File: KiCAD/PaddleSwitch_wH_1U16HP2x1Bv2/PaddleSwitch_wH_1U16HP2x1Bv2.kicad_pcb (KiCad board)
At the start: 2 copper layers, 80.9 x 39.7 mm, 13 parts, among them SW1 SW_DPDT-p5xp6i_Panel_Mount_Pa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, SW2 SW_DPDT-p5xp6i_Panel_Mount_Pa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

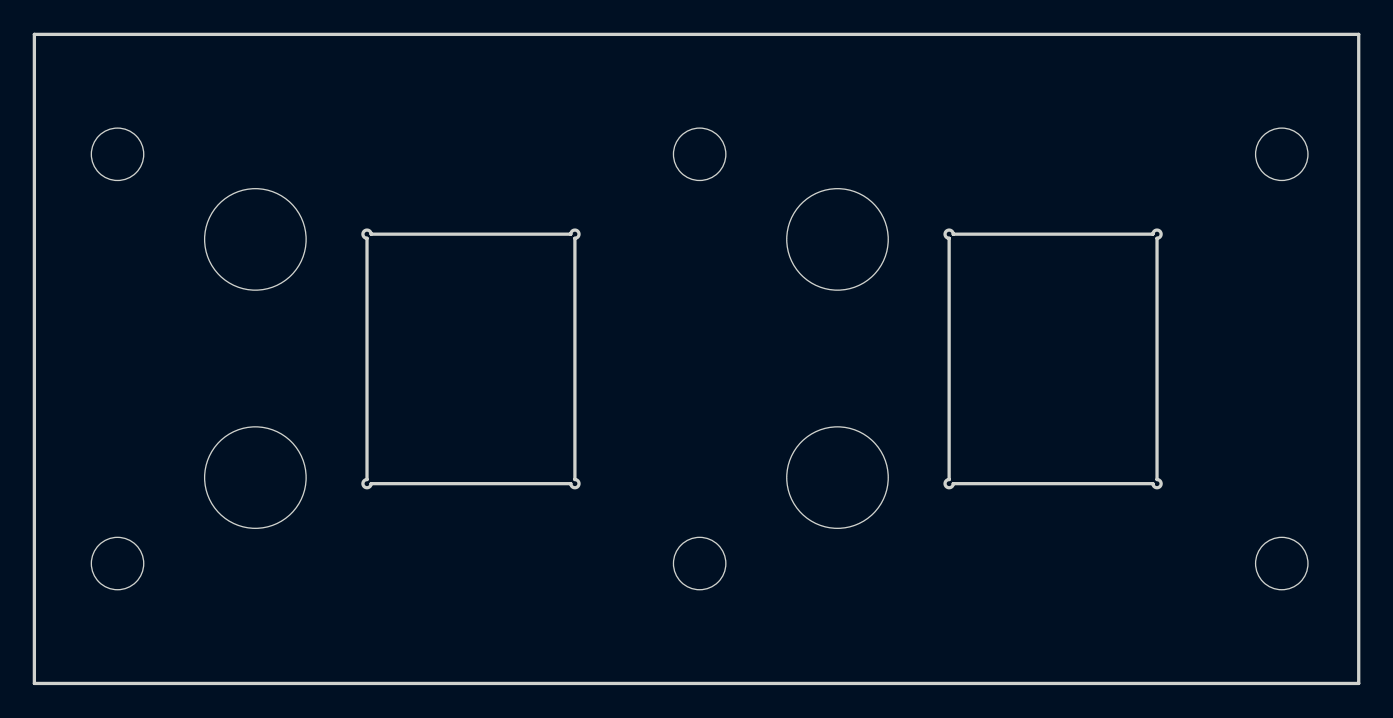
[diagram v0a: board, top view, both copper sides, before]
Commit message: updated all modules to use plated through-holes wherever possible
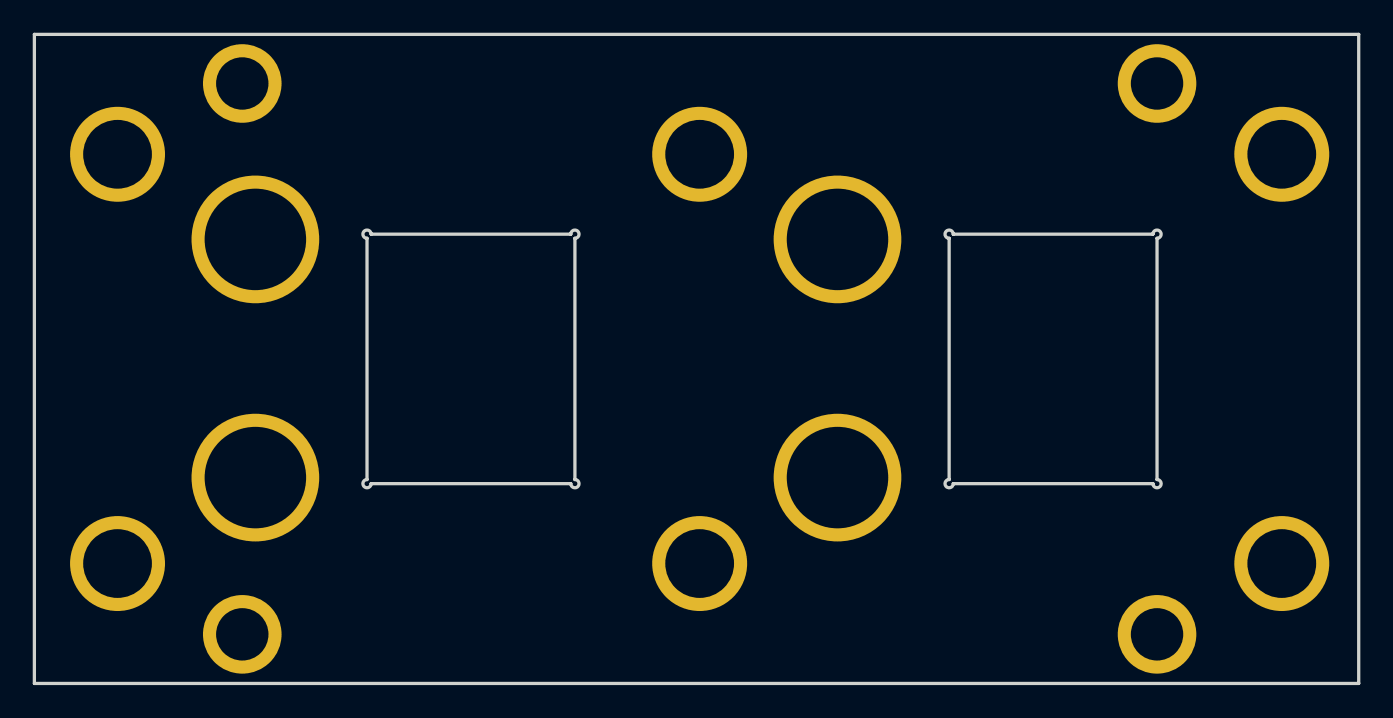
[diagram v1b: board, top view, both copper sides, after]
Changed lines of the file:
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@@
 			)
 		)
-		(pad "" np_thru_hole oval
+		(pad "" thru_hole circle
 			(at 0 0)
-			(size 4.34 3.2)
-			(drill oval 4.34 3.2)
+			(size 4.8 4.8)
+			(drill 3.2)
 			(layers "*.Cu" "*.Mask")
+			(remove_unused_layers no)
 		)
 		(embedded_fonts no)
@@
 			)
 		)
-		(pad "" np_thru_hole oval
+		(pad "" thru_hole circle
 			(at 0 0)
-			(size 4.34 3.2)
-			(drill oval 4.34 3.2)
+			(size 4.8 4.8)
+			(drill 3.2)
 			(layers "*.Cu" "*.Mask")
+			(remove_unused_layers no)
 		)
 		(embedded_fonts no)
@@
 			)
 		)
-		(pad "" np_thru_hole circle
+		(pad "" thru_hole circle
 			(at 0 0)
-			(size 6.2 6.2)
+			(size 7.8 7.8)
 			(drill 6.2)
 			(layers "*.Cu" "*.Mask")
+			(remove_unused_layers no)
 		)
 		(embedded_fonts no)
@@
 			)
 		)
+		(property "Source" "https://www.aliexpress.com/item/1005007242440186.html"
+			(at 0 36 0)
+			(layer "F.Fab")
+			(hide yes)
+			(effects
+				(font
+					(size 1 1)
+					(thickness 0.1)
+				)
+			)
+		)
 		(sheetname "/")
 		(sheetfile "PaddleSwitch_wH_1U16HP2x1Bv2.kicad_sch")
@@
 			)
 		)
-		(pad "" np_thru_hole circle
+		(pad "" thru_hole circle
 			(at 0 0)
-			(size 3.2 3.2)
-			(drill 3.2)
+			(size 5.8 5.8)
+			(drill 4.2)
 			(layers "*.Cu" "*.Mask")
-		)
-		(pad "" np_thru_hole circle
+			(remove_unused_layers no)
+		)
+		(pad "" thru_hole circle
 			(at 0 25)
-			(size 3.2 3.2)
-			(drill 3.2)
+			(size 5.8 5.8)
+			(drill 4.2)
 			(layers "*.Cu" "*.Mask")
+			(remove_unused_layers no)
 		)
 		(embedded_fonts no)
@@
 			)
 		)
-		(pad "" np_thru_hole circle
+		(pad "" thru_hole circle
 			(at 0 0)
-			(size 6.2 6.2)
+			(size 7.8 7.8)
 			(drill 6.2)
 			(layers "*.Cu" "*.Mask")
+			(remove_unused_layers no)
 		)
 		(embedded_fonts no)
@@
 			)
 		)
+		(property "Source" "https://www.aliexpress.com/item/1005007242440186.html"
+			(at 0 36 0)
+			(layer "F.Fab")
+			(hide yes)
+			(effects
+				(font
+					(size 1 1)
+					(thickness 0.1)
+				)
+			)
+		)
 		(sheetname "/")
 		(sheetfile "PaddleSwitch_wH_1U16HP2x1Bv2.kicad_sch")
@@
 			)
 		)
-		(pad "" np_thru_hole circle
+		(pad "" thru_hole circle
 			(at 0 0)
-			(size 3.2 3.2)
-			(drill 3.2)
+			(size 5.8 5.8)
+			(drill 4.2)
 			(layers "*.Cu" "*.Mask")
-		)
-		(pad "" np_thru_hole circle
+			(remove_unused_layers no)
+		)
+		(pad "" thru_hole circle
 			(at 0 25)
-			(size 3.2 3.2)
-			(drill 3.2)
+			(size 5.8 5.8)
+			(drill 4.2)
 			(layers "*.Cu" "*.Mask")
+			(remove_unused_layers no)
 		)
 		(embedded_fonts no)
@@
 			)
 		)
-		(pad "" np_thru_hole circle
+		(pad "" thru_hole circle
 			(at 0 0)
-			(size 6.2 6.2)
+			(size 7.8 7.8)
 			(drill 6.2)
 			(layers "*.Cu" "*.Mask")
+			(remove_unused_layers no)
 		)
 		(embedded_fonts no)
@@
 			)
 		)
-		(pad "" np_thru_hole circle
+		(pad "" thru_hole circle
 			(at 0 0)
-			(size 6.2 6.2)
+			(size 7.8 7.8)
 			(drill 6.2)
 			(layers "*.Cu" "*.Mask")
+			(remove_unused_layers no)
 		)
 		(embedded_fonts no)
@@
 			)
 		)
-		(pad "" np_thru_hole oval
+		(pad "" thru_hole circle
 			(at 0 0)
-			(size 4.34 3.2)
-			(drill oval 4.34 3.2)
+			(size 4.8 4.8)
+			(drill 3.2)
 			(layers "*.Cu" "*.Mask")
+			(remove_unused_layers no)
 		)
 		(embedded_fonts no)
@@
 			)
 		)
+		(property "Source" "https://www.aliexpress.com/item/1005007242440186.html"
+			(at 0 36 0)
+			(layer "F.Fab")
+			(hide yes)
+			(effects
+				(font
+					(size 1 1)
+					(thickness 0.1)
+				)
+			)
+		)
 		(sheetname "/")
 		(sheetfile "PaddleSwitch_wH_1U16HP2x1Bv2.kicad_sch")
@@
 			)
 		)
-		(pad "" np_thru_hole circle
+		(pad "" thru_hole circle
 			(at 0 0)
-			(size 3.2 3.2)
-			(drill 3.2)
+			(size 5.8 5.8)
+			(drill 4.2)
 			(layers "*.Cu" "*.Mask")
-		)
-		(pad "" np_thru_hole circle
+			(remove_unused_layers no)
+		)
+		(pad "" thru_hole circle
 			(at 0 25)
-			(size 3.2 3.2)
-			(drill 3.2)
+			(size 5.8 5.8)
+			(drill 4.2)
 			(layers "*.Cu" "*.Mask")
+			(remove_unused_layers no)
 		)
 		(embedded_fonts no)
@@
 			)
 		)
-		(pad "" np_thru_hole oval
+		(pad "" thru_hole circle
 			(at 0 0)
-			(size 4.34 3.2)
-			(drill oval 4.34 3.2)
+			(size 4.8 4.8)
+			(drill 3.2)
 			(layers "*.Cu" "*.Mask")
+			(remove_unused_layers no)
 		)
 		(embedded_fonts no)
